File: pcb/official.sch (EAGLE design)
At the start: 16 parts, among them P1 DEV_CLP-150, P8 DEV_1X40

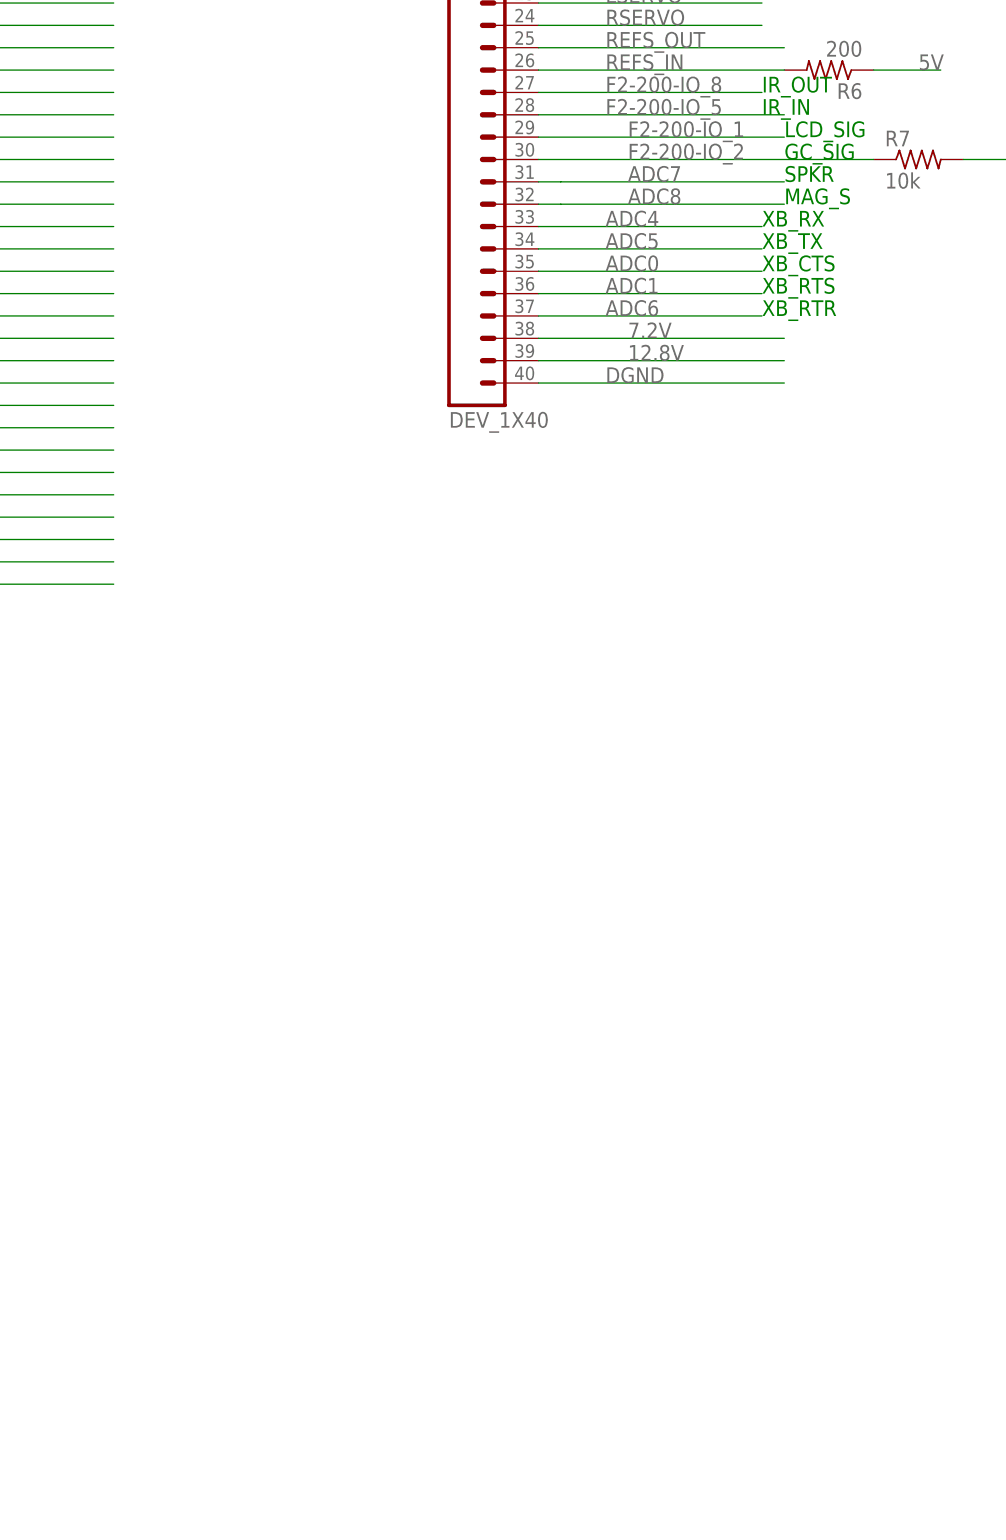
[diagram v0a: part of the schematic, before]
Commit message: Added sound amp to pcb design file
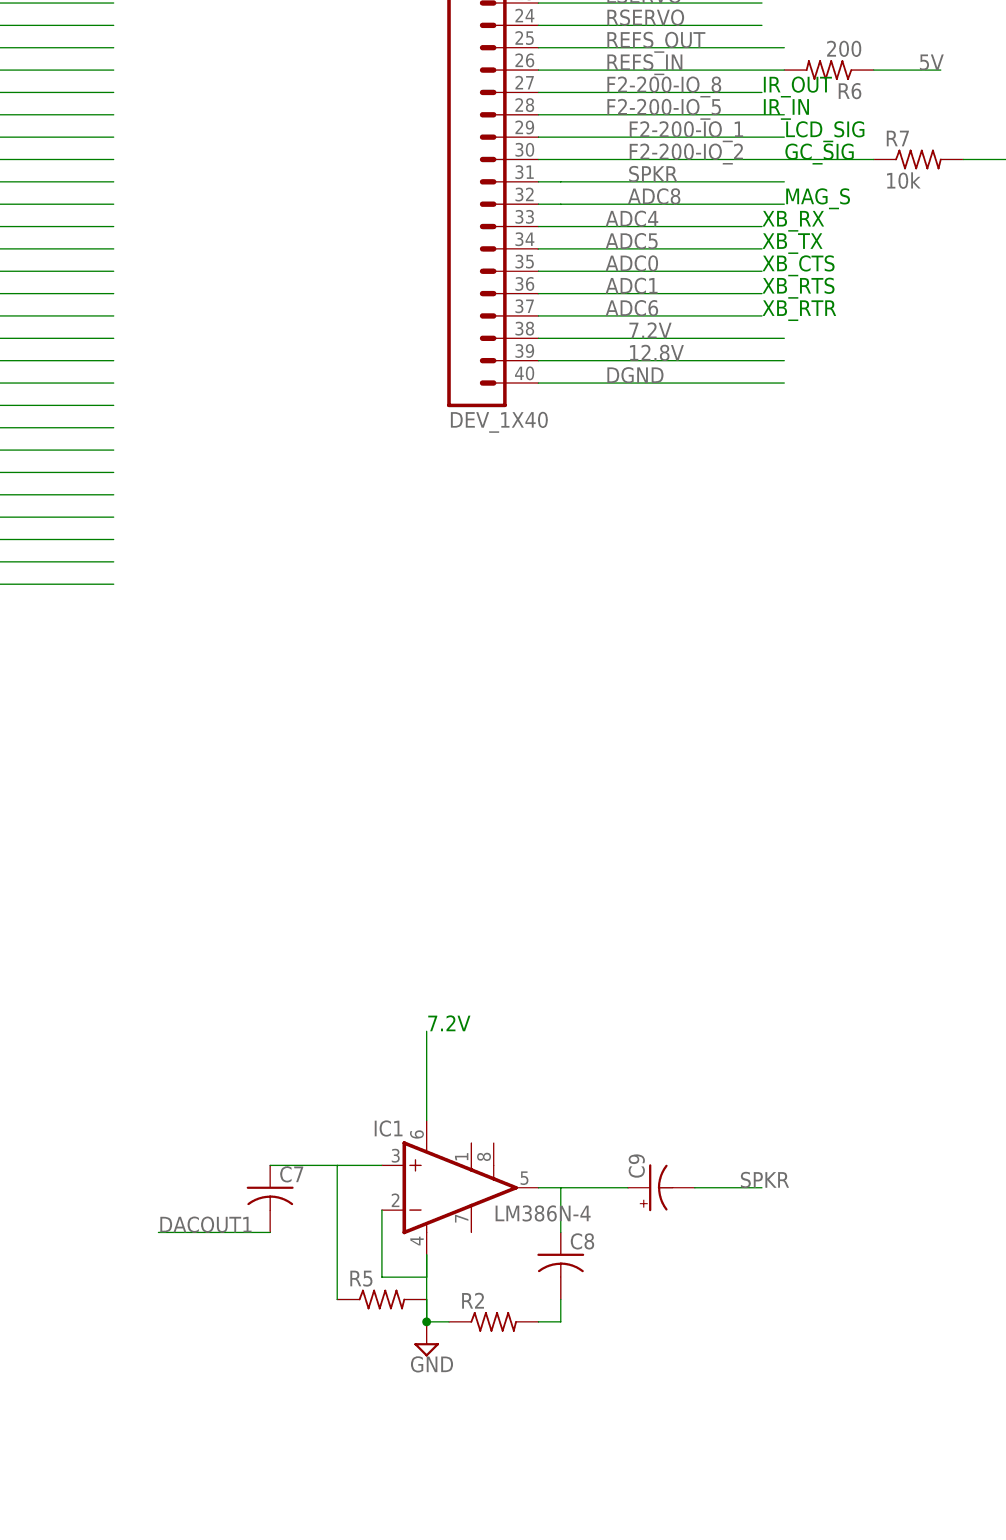
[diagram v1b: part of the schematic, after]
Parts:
- added C7: (no value), rcl:C-US075-032X103
- added C8: (no value), rcl:C-US025-025X050
- added C9: (no value), rcl:CPOL-USB45181B
- added IC1: LM386N-4, linear:LM386N-4
- added R2, R5: (no value), rcl:R-US_0207/12
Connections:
- new net N$2: C7.1, IC1.+IN, R5.1
- new net N$4: C8.2, R2.2
- new net N$5: C8.1, C9.+, IC1.OUT
- new net N$6: IC1.VS
- new net SPKR: C9.-, P8.31
- net ADC7: no longer P8.31
- net DACOUT1: now also C7.2
- net GND: now also IC1.-IN, IC1.GND, R2.1, R5.2
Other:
- note added: "7.2V"
- note removed: "SPKR"
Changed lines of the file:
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@@
 <part name="R6" library="rcl" deviceset="R-US_" device="0309/12" value="200"/>
 <part name="R7" library="rcl" deviceset="R-US_" device="0309/12" value="10k"/>
+<part name="R2" library="rcl" deviceset="R-US_" device="0207/12"/>
+<part name="IC1" library="linear" deviceset="LM386?-*" device="N" technology="4" value="LM386N-4"/>
+<part name="C7" library="rcl" deviceset="C-US" device="075-032X103"/>
+<part name="C8" library="rcl" deviceset="C-US" device="025-025X050"/>
+<part name="SUPPLY4" library="supply2" deviceset="GND" device=""/>
+<part name="R5" library="rcl" deviceset="R-US_" device="0207/12"/>
+<part name="C9" library="rcl" deviceset="CPOL-US" device="B45181B"/>
 </parts>
 <sheets>
@@
 <text x="104.14" y="15.24" size="1.778" layer="91">IR_IN</text>
 <text x="104.14" y="17.78" size="1.778" layer="91">IR_OUT</text>
-<text x="106.68" y="7.62" size="1.778" layer="91">SPKR</text>
 <text x="106.68" y="5.08" size="1.778" layer="91">MAG_S</text>
+<text x="66.04" y="-88.9" size="1.778" layer="91">7.2V</text>
 </plain>
 <instances>
@@
 <instance part="R6" gate="G$1" x="111.76" y="20.32" rot="R180"/>
 <instance part="R7" gate="G$1" x="121.92" y="10.16"/>
+<instance part="R2" gate="G$1" x="73.66" y="-121.92"/>
+<instance part="IC1" gate="G$1" x="68.58" y="-106.68"/>
+<instance part="C7" gate="G$1" x="48.26" y="-106.68"/>
+<instance part="C8" gate="G$1" x="81.28" y="-114.3"/>
+<instance part="SUPPLY4" gate="GND" x="66.04" y="-124.46"/>
+<instance part="R5" gate="G$1" x="60.96" y="-119.38"/>
+<instance part="C9" gate="G$1" x="91.44" y="-106.68" rot="R90"/>
 </instances>
 <busses>
@@
 <pinref part="P1" gate="G$1" pin="P$46"/>
 </segment>
+<segment>
+<pinref part="C7" gate="G$1" pin="2"/>
+<wire x1="48.26" y1="-111.76" x2="35.56" y2="-111.76" width="0.1524" layer="91"/>
+<label x="35.56" y="-111.76" size="1.778" layer="95"/>
+</segment>
 </net>
 <net name="ADC10" class="0">
@@
 <label x="-60.96" y="-15.24" size="1.778" layer="95"/>
 <pinref part="P1" gate="G$1" pin="P$82"/>
-</segment>
-<segment>
-<wire x1="81.28" y1="7.62" x2="106.68" y2="7.62" width="0.2032" layer="91"/>
-<label x="88.9" y="7.62" size="1.778" layer="95"/>
-<pinref part="P8" gate="G$1" pin="31"/>
-<wire x1="81.28" y1="7.62" x2="78.74" y2="7.62" width="0.1524" layer="91"/>
 </segment>
 </net>
@@
 <pinref part="LM219" gate="G$1" pin="8"/>
 </segment>
+<segment>
+<pinref part="IC1" gate="G$1" pin="-IN"/>
+<wire x1="60.96" y1="-109.22" x2="60.96" y2="-116.84" width="0.1524" layer="91"/>
+<wire x1="60.96" y1="-116.84" x2="66.04" y2="-116.84" width="0.1524" layer="91"/>
+<pinref part="IC1" gate="G$1" pin="GND"/>
+<wire x1="66.04" y1="-116.84" x2="66.04" y2="-114.3" width="0.1524" layer="91"/>
+<pinref part="SUPPLY4" gate="GND" pin="GND"/>
+<wire x1="66.04" y1="-114.3" x2="66.04" y2="-121.92" width="0.1524" layer="91"/>
+<pinref part="R5" gate="G$1" pin="2"/>
+<junction x="66.04" y="-121.92"/>
+<wire x1="66.04" y1="-121.92" x2="66.04" y2="-119.38" width="0.1524" layer="91"/>
+<pinref part="R2" gate="G$1" pin="1"/>
+<wire x1="66.04" y1="-121.92" x2="68.58" y2="-121.92" width="0.1524" layer="91"/>
+</segment>
 </net>
 <net name="LMOTOR" class="0">
@@
 </segment>
 </net>
+<net name="N$2" class="0">
+<segment>
+<pinref part="IC1" gate="G$1" pin="+IN"/>
+<pinref part="C7" gate="G$1" pin="1"/>
+<wire x1="60.96" y1="-104.14" x2="55.88" y2="-104.14" width="0.1524" layer="91"/>
+<pinref part="R5" gate="G$1" pin="1"/>
+<wire x1="55.88" y1="-104.14" x2="48.26" y2="-104.14" width="0.1524" layer="91"/>
+<wire x1="55.88" y1="-119.38" x2="55.88" y2="-104.14" width="0.1524" layer="91"/>
+</segment>
+</net>
+<net name="N$4" class="0">
+<segment>
+<pinref part="R2" gate="G$1" pin="2"/>
+<pinref part="C8" gate="G$1" pin="2"/>
+<wire x1="78.74" y1="-121.92" x2="81.28" y2="-121.92" width="0.1524" layer="91"/>
+<wire x1="81.28" y1="-121.92" x2="81.28" y2="-119.38" width="0.1524" layer="91"/>
+</segment>
+</net>
+<net name="N$5" class="0">
+<segment>
+<pinref part="IC1" gate="G$1" pin="OUT"/>
+<pinref part="C8" gate="G$1" pin="1"/>
+<wire x1="78.74" y1="-106.68" x2="81.28" y2="-106.68" width="0.1524" layer="91"/>
+<wire x1="81.28" y1="-106.68" x2="81.28" y2="-111.76" width="0.1524" layer="91"/>
+<pinref part="C9" gate="G$1" pin="+"/>
+<wire x1="81.28" y1="-106.68" x2="88.9" y2="-106.68" width="0.1524" layer="91"/>
+</segment>
+</net>
+<net name="N$6" class="0">
+<segment>
+<pinref part="IC1" gate="G$1" pin="VS"/>
+<wire x1="66.04" y1="-99.06" x2="66.04" y2="-88.9" width="0.1524" layer="91"/>
+</segment>
+</net>
+<net name="SPKR" class="0">
+<segment>
+<wire x1="81.28" y1="7.62" x2="106.68" y2="7.62" width="0.2032" layer="91"/>
+<label x="88.9" y="7.62" size="1.778" layer="95"/>
+<pinref part="P8" gate="G$1" pin="31"/>
+<wire x1="81.28" y1="7.62" x2="78.74" y2="7.62" width="0.1524" layer="91"/>
+</segment>
+<segment>
+<pinref part="C9" gate="G$1" pin="-"/>
+<wire x1="96.52" y1="-106.68" x2="104.14" y2="-106.68" width="0.1524" layer="91"/>
+<label x="101.6" y="-106.68" size="1.778" layer="95"/>
+</segment>
+</net>

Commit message: Better pcb
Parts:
- removed C1, C2, C3, C4, C5, C6: (no value), SparkFun:CAP0603-CAP
- removed IC1: LM386N-4, linear:LM386N-4
- removed LM219: (no value), ic-package:DIL14S
- removed P8: DEV_1X40, EECS370:DEV_1X40
- removed VOLT_REG: REG1117F, burr-brown:REG1117F
- added C10, C11, C12, C15: (no value), rcl:CPOL-USB45181B
- added C13: (no value), rcl:C-US075-032X103
- added C14: (no value), rcl:C-US025-025X050
- added COMPARATOR: (no value), ic-package:DIL14S
- added OPAMP: LM386N-4, linear:LM386N-4
- added P11: DEV_1X40, EECS370:DEV_1X40
- added R8: 750, rcl:R-US_0309/12
- added R9: 10, rcl:R-US_0309/12
- added VREG: 7806T, linear:7806T
- C7: device rcl:C-US075-032X103 -> rcl:CPOL-USB45181B
- C8: device rcl:C-US025-025X050 -> rcl:CPOL-USB45181B
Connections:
- removed net 5V: H-BRIDGE1.ENABLE_B, H-BRIDGE1.VCC, LM219.11, R1.2, R3.1, R4.1, R6.1, VOLT_REG.VOUT
- removed net GND: H-BRIDGE1.GND, H-BRIDGE1.SEN_A, H-BRIDGE1.SEN_B, IC1.-IN, IC1.GND, LM219.3, LM219.6, LM219.8, R2.1, R5.2, VOLT_REG.GND
- new net ADC11: P1.P$90
- new net ADC9: P1.P$86
- new net MSS_GPIO_5: P11.39
- new net MSS_GPIO_6: P11.40
- new net N$1: H-BRIDGE1.OUT3, R9.2
- net 12.8V: no longer P8.39
- net 7.2V: now also VREG.VI; no longer P8.38, VOLT_REG.VIN
- net ADC0: no longer P8.35
- net ADC1: no longer P8.36
- net ADC4: no longer P8.33
- net ADC5: no longer P8.34
- net ADC6: no longer P8.37
- net ADC8: no longer P8.32
- net AGND: now also P1.P$88, P1.P$92, P1.P$94
- net DACOUT1: now also C13.2; no longer C7.2
- net DGND: now also C10.-, C11.-, C12.-, C7.-, C8.-, C9.-, COMPARATOR.3, COMPARATOR.6, COMPARATOR.8, H-BRIDGE1.GND, H-BRIDGE1.SEN_A, H-BRIDGE1.SEN_B, OPAMP.-IN, OPAMP.GND, P1.P$96, P11.9, R2.1, R5.2, VREG.GND; no longer C1.2, C2.2, C3.2, C4.2, C5.2, C6.2, P8.20, P8.3, P8.40
- net F2-200-IO_0: now also P11.30; no longer H-BRIDGE1.ENABLE_A
- net F2-200-IO_1: now also P11.31; no longer P8.29
- net F2-200-IO_2: now also P11.32; no longer P8.30, R7.1
- net F2-200-IO_3: now also P11.33, R7.1; no longer H-BRIDGE1.INPUT1
- net F2-200-IO_4: now also H-BRIDGE1.ENABLE_A; no longer H-BRIDGE1.INPUT2
- net F2-200-IO_5: now also H-BRIDGE1.INPUT1; no longer P8.28
- net F2-200-IO_6: now also H-BRIDGE1.INPUT2; no longer H-BRIDGE1.INPUT3
- net F2-200-IO_7: now also H-BRIDGE1.INPUT3; no longer H-BRIDGE1.INPUT4
- net F2-200-IO_8: now also H-BRIDGE1.INPUT4; no longer P8.27
- net LMOTOR: now also P11.24; no longer P8.21
- net LSERVO: now also P11.26, R9.1; no longer H-BRIDGE1.OUT3, P8.23
- net MSS_GP_IO_0: now also P11.35, R8.2; no longer P8.4
- net MSS_GP_IO_1: now also COMPARATOR.12, R1.1; no longer P8.5
- net MSS_GP_IO_10: now also P11.18; no longer P8.14
- net MSS_GP_IO_11: now also P11.19; no longer P8.15
- net MSS_GP_IO_12: now also P11.20; no longer P8.16
- net MSS_GP_IO_13: now also P11.21; no longer P8.17
- net MSS_GP_IO_14: now also P11.22; no longer P8.18
- net MSS_GP_IO_15: now also P11.23; no longer P8.19
- net MSS_GP_IO_2: now also P11.36; no longer LM219.12, R1.1
- net MSS_GP_IO_3: now also P11.37; no longer P8.7
- net MSS_GP_IO_4: now also P11.38; no longer P8.8
- net MSS_GP_IO_5: no longer P8.9
- net MSS_GP_IO_6: no longer P8.10
- net MSS_GP_IO_7: now also P11.15; no longer P8.11
- net MSS_GP_IO_8: now also P11.16; no longer P8.12
- net MSS_GP_IO_9: now also P11.17; no longer P8.13
- net N$2: now also C13.1, OPAMP.+IN; no longer C7.1, IC1.+IN
- net N$3: now also COMPARATOR.5; no longer LM219.5
- net N$4: now also C14.2; no longer C8.2
- net N$5: now also C14.1, C15.+, OPAMP.OUT; no longer C8.1, C9.+, IC1.OUT
- net N$6: now also OPAMP.VS; no longer IC1.VS
- net REFS_IN: now also COMPARATOR.4, P11.28, R3.2; no longer P8.26, R6.2
- net REFS_OUT: now also P11.29, R6.2; no longer LM219.4, P8.25, R3.2
- net RMOTOR: now also P11.25; no longer P8.22
- net RSERVO: now also P11.27; no longer P8.24
- net SPKR: now also C15.-, P11.34; no longer C9.-, P8.31
- net VDD3.3: now also C10.+, C11.+, C12.+, P1.P$100, P1.P$98, P11.14; no longer C4.1, C5.1, C6.1, P8.2
- net VDD5: now also C7.+, C8.+, C9.+, COMPARATOR.11, H-BRIDGE1.ENABLE_B, H-BRIDGE1.VCC, P11.1, P11.4, R1.2, R3.1, R4.1, R6.1, R8.1, VREG.VO; no longer C1.1, C2.1, C3.1, P8.1
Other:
- note added: "UMKARTS Board"
- note removed: "UMKART Extension board"
- moved on the sheet: C9, H-BRIDGE1, P1, R1, R2, R3, R4, R5, R6, R7

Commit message: Rough draft
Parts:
- removed R6: 200, rcl:R-US_0309/12
- removed R7: 10k, rcl:R-US_0309/12
- removed R8: 750, rcl:R-US_0309/12
- added R10: 200, rcl:R-US_0309/12
- added R11: 10k, rcl:R-US_0309/12
- added R12: 750, rcl:R-US_0309/12
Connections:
- net 12.8V: now also P11.8
- net 7.2V: now also P11.5
- net DGND: now also P11.10, P11.11, P11.12, P11.6, P11.7
- net F2-200-IO_0: now also P11.21; no longer P11.30
- net F2-200-IO_1: now also P11.22; no longer P11.31
- net F2-200-IO_2: now also P11.23; no longer P11.32
- net F2-200-IO_3: now also P11.24, R11.1; no longer P11.33, R7.1
- net LMOTOR: now also P11.15; no longer P11.24
- net LSERVO: now also P11.17; no longer P11.26
- net MSS_GPIO_5: now also P11.30; no longer P11.39
- net MSS_GPIO_6: now also P11.31; no longer P11.40
- net MSS_GP_IO_0: now also P11.26, R12.2; no longer P11.35, R8.2
- net MSS_GP_IO_10: now also P11.35; no longer P11.18
- net MSS_GP_IO_11: now also P11.36; no longer P11.19
- net MSS_GP_IO_12: now also P11.37; no longer P11.20
- net MSS_GP_IO_13: now also P11.38; no longer P11.21
- net MSS_GP_IO_14: now also P11.39; no longer P11.22
- net MSS_GP_IO_15: now also P11.40; no longer P11.23
- net MSS_GP_IO_2: now also P11.27; no longer P11.36
- net MSS_GP_IO_3: now also P11.28; no longer P11.37
- net MSS_GP_IO_4: now also P11.29; no longer P11.38
- net MSS_GP_IO_7: now also P11.32; no longer P11.15
- net MSS_GP_IO_8: now also P11.33; no longer P11.16
- net MSS_GP_IO_9: now also P11.34; no longer P11.17
- net REFS_IN: now also P11.19; no longer P11.28
- net REFS_OUT: now also P11.20, R10.2; no longer P11.29, R6.2
- net RMOTOR: now also P11.16; no longer P11.25
- net RSERVO: now also P11.18; no longer P11.27
- net SPKR: now also P11.25; no longer P11.34
- net VDD3.3: now also P11.13, R11.2; no longer R7.2
- net VDD5: now also P11.2, P11.3, R10.1, R12.1; no longer R6.1, R8.1
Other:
- moved on the sheet: P11, R9

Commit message: New kyle resistor
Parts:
- added R6: (no value), rcl:R-US_0207/12
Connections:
- new net N$9: C13.2, R6.2
- net 12.8V: no longer P11.8
- net 7.2V: no longer P11.5
- net DACOUT1: now also R6.1; no longer C13.2
- net DGND: no longer P11.10, P11.11, P11.6, P11.7
- net VDD5: no longer P11.2, P11.3
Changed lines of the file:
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@@
 <part name="R11" library="rcl" deviceset="R-US_" device="0309/12" value="10k"/>
 <part name="R12" library="rcl" deviceset="R-US_" device="0309/12" value="750"/>
+<part name="R6" library="rcl" deviceset="R-US_" device="0207/12"/>
 </parts>
 <sheets>
@@
 <instance part="R11" gate="G$1" x="106.68" y="22.86"/>
 <instance part="R12" gate="G$1" x="111.76" y="17.78" rot="R180"/>
+<instance part="R6" gate="G$1" x="106.68" y="-106.68"/>
 </instances>
 <busses>
@@
 </segment>
 <segment>
-<wire x1="50.8" y1="66.04" x2="71.12" y2="66.04" width="0.1524" layer="91"/>
+<wire x1="55.88" y1="66.04" x2="71.12" y2="66.04" width="0.1524" layer="91"/>
 <label x="78.74" y="66.04" size="1.778" layer="95"/>
 <wire x1="71.12" y1="66.04" x2="96.52" y2="66.04" width="0.1524" layer="91"/>
-<wire x1="50.8" y1="68.58" x2="71.12" y2="68.58" width="0.1524" layer="91"/>
+<wire x1="55.88" y1="68.58" x2="71.12" y2="68.58" width="0.1524" layer="91"/>
 <wire x1="71.12" y1="68.58" x2="71.12" y2="66.04" width="0.1524" layer="91"/>
 <junction x="71.12" y="66.04"/>
@@
 <wire x1="106.68" y1="60.96" x2="96.52" y2="60.96" width="0.1524" layer="91"/>
 <wire x1="96.52" y1="60.96" x2="96.52" y2="66.04" width="0.1524" layer="91"/>
-<pinref part="P11" gate="G$1" pin="7"/>
-<pinref part="P11" gate="G$1" pin="6"/>
 </segment>
 <segment>
@@
 <wire x1="55.88" y1="58.42" x2="83.82" y2="58.42" width="0.2032" layer="91"/>
 <label x="71.12" y="58.42" size="1.778" layer="95"/>
-<pinref part="P11" gate="G$1" pin="10"/>
-<wire x1="55.88" y1="58.42" x2="50.8" y2="58.42" width="0.1524" layer="91"/>
 </segment>
 <segment>
 <wire x1="55.88" y1="55.88" x2="83.82" y2="55.88" width="0.2032" layer="91"/>
 <label x="68.58" y="55.88" size="1.778" layer="95"/>
-<pinref part="P11" gate="G$1" pin="11"/>
-<wire x1="55.88" y1="55.88" x2="50.8" y2="55.88" width="0.1524" layer="91"/>
 </segment>
 <segment>
@@
 </segment>
 <segment>
-<pinref part="C13" gate="G$1" pin="2"/>
-<wire x1="114.3" y1="-106.68" x2="101.6" y2="-106.68" width="0.1524" layer="91"/>
-<label x="101.6" y="-106.68" size="1.778" layer="95"/>
+<label x="86.36" y="-106.68" size="1.778" layer="95"/>
+<pinref part="R6" gate="G$1" pin="1"/>
+<wire x1="101.6" y1="-106.68" x2="86.36" y2="-106.68" width="0.1524" layer="91"/>
 </segment>
 </net>
@@
 <label x="63.5" y="78.74" size="1.778" layer="95"/>
 <label x="63.5" y="76.2" size="1.778" layer="95"/>
-<pinref part="P11" gate="G$1" pin="3"/>
-<wire x1="55.88" y1="76.2" x2="50.8" y2="76.2" width="0.1524" layer="91"/>
-<pinref part="P11" gate="G$1" pin="2"/>
-<wire x1="55.88" y1="78.74" x2="50.8" y2="78.74" width="0.1524" layer="91"/>
 </segment>
 <segment>
@@
 <segment>
 <pinref part="VREG" gate="A1" pin="VI"/>
+<wire x1="96.52" y1="71.12" x2="88.9" y2="71.12" width="0.1524" layer="91"/>
 <label x="91.44" y="71.12" size="1.778" layer="95"/>
-<wire x1="50.8" y1="71.12" x2="96.52" y2="71.12" width="0.1524" layer="91"/>
+<wire x1="55.88" y1="71.12" x2="86.36" y2="71.12" width="0.1524" layer="91"/>
 <label x="78.74" y="71.12" size="1.778" layer="95"/>
-<pinref part="P11" gate="G$1" pin="5"/>
+<wire x1="86.36" y1="71.12" x2="88.9" y2="71.12" width="0.1524" layer="91"/>
 </segment>
 </net>
@@
 </segment>
 <segment>
-<wire x1="50.8" y1="63.5" x2="101.6" y2="63.5" width="0.1524" layer="91"/>
+<wire x1="55.88" y1="63.5" x2="101.6" y2="63.5" width="0.1524" layer="91"/>
 <label x="78.74" y="63.5" size="1.778" layer="95"/>
-<pinref part="P11" gate="G$1" pin="8"/>
 </segment>
 </net>
@@
 </segment>
 </net>
+<net name="N$9" class="0">
+<segment>
+<pinref part="C13" gate="G$1" pin="2"/>
+<wire x1="114.3" y1="-106.68" x2="111.76" y2="-106.68" width="0.1524" layer="91"/>
+<pinref part="R6" gate="G$1" pin="2"/>
+</segment>
+</net>
